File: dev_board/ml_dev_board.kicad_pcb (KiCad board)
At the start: 2 copper layers, 100 x 73.2 mm, 55 parts, among them J1 JTAG 3.3V, J2 Canon-Service-Connector, J3 USB_B_Mini, J4 Probe Connector, J5 canon_service_jumper_terminal, Q1 IRLML5203, U1 SN74AUP1T34DCK, U2 SN74AUP1T34DCK, U3 93LCxxBxxOT, U4 LD1117S33TR_SOT223, U5 FT4232H, U6 74HC595, Y1 12MHz

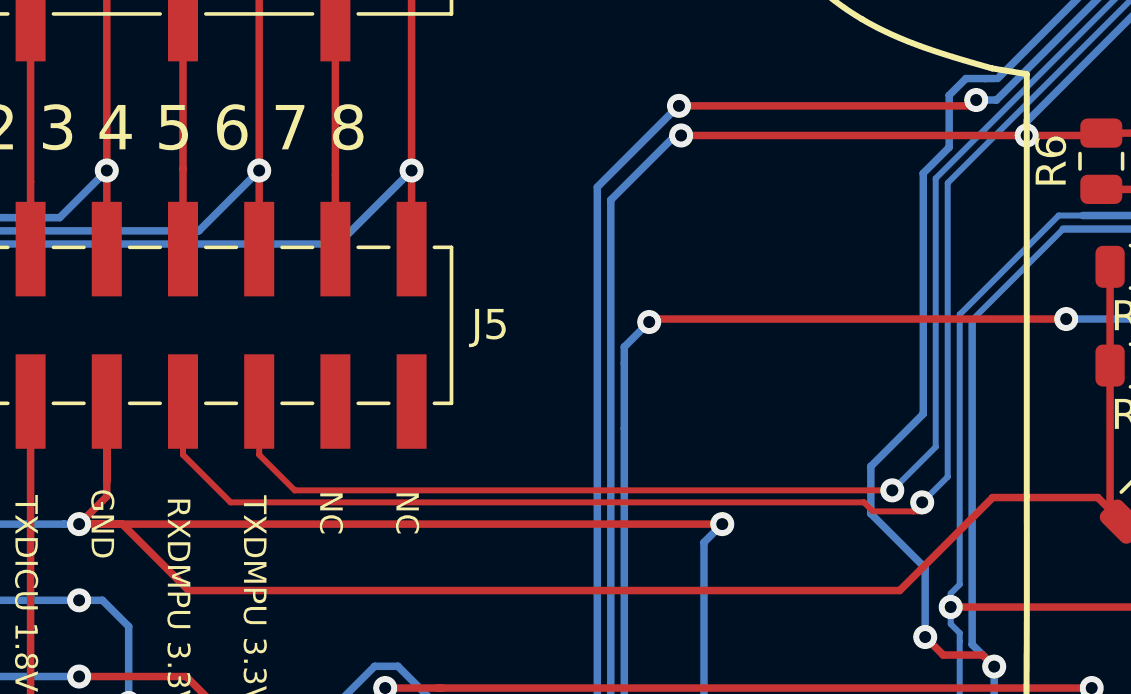
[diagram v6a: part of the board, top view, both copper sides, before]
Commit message: dev board: jumper terminal: move RXMPU from pin 5 to pin 7
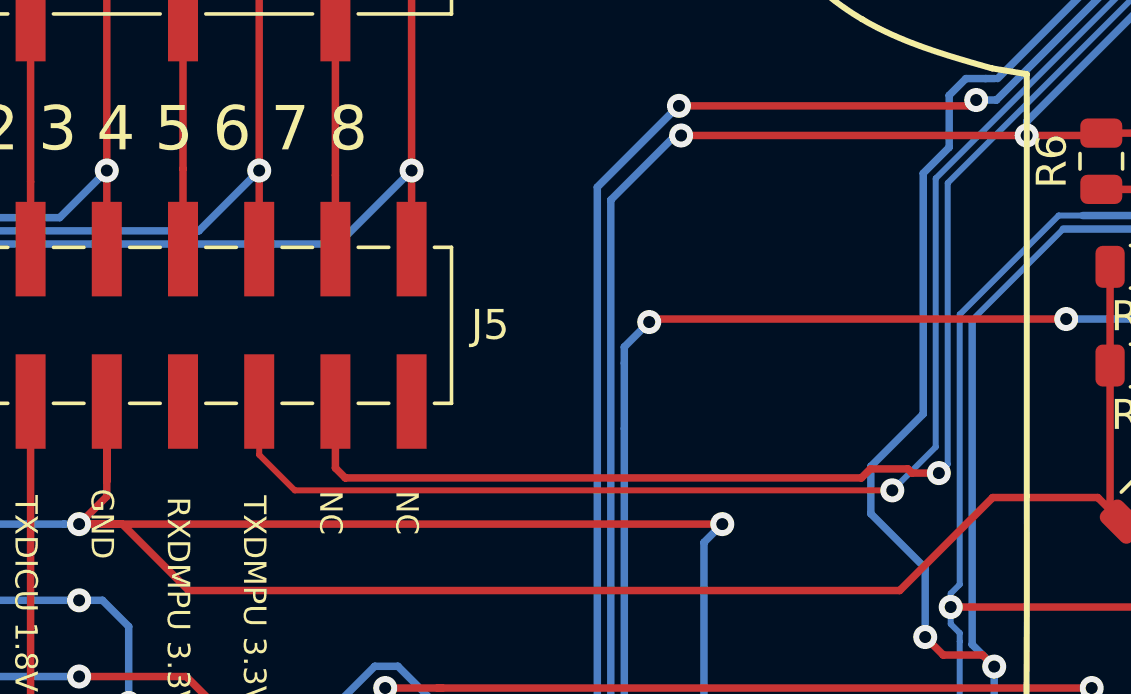
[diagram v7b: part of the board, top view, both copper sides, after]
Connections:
- J5 pad 15: /RXDMPU -> (no net)
- J5 pad 17: (no net) -> /RXDMPU
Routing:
- net /RXDMPU: track 70.0 -> 63.7 mm

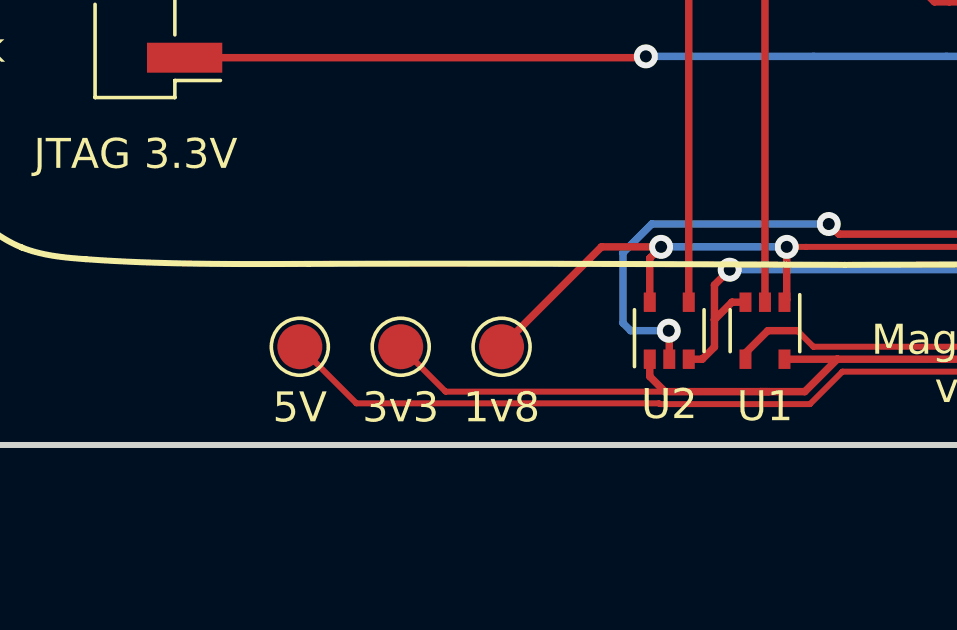
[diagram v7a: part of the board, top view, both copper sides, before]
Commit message: dev board: add 1v8 pullup resistor to TXICU pin
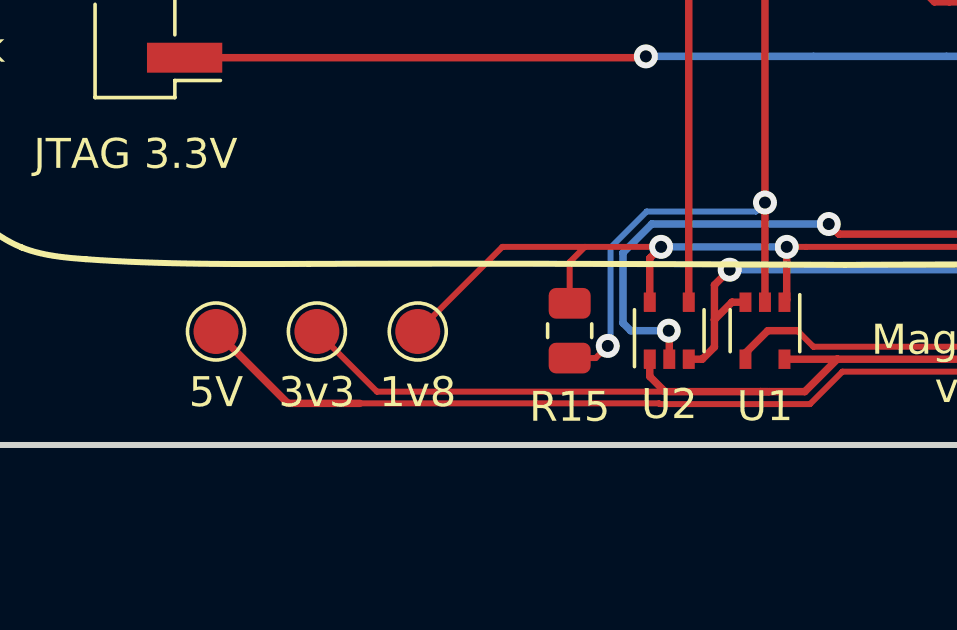
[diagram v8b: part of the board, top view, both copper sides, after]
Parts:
- added R15: 1K, Resistor_SMD:R_0805_2012Metric, F.Cu at (115.6, 116.8)
- moved TP1 2.84 mm to (103.8, 116.9)
- moved TP2 2.84 mm to (110.5, 116.9)
- moved TP3 2.84 mm to (107.1, 116.9)
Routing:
- net /TXDICU_1V8: track 22.4 -> 33.0 mm, vias 0 -> 2
- net +1V8: track 145.6 -> 150.3 mm
- net +5V: track 163.7 -> 166.8 mm
- net +3V3: track 211.0 -> 214.0 mm
